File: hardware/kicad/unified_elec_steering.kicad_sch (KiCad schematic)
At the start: 18 parts, among them J1 Conn_01x03, J10 Conn_01x04, J11 Conn_01x03, J13 Conn_01x03, J2 Conn_01x03, J3 Conn_01x05, J4 Conn_01x03, J5 Conn_01x03, J6 Conn_01x02, J7 Conn_01x04, J8 Conn_01x12, J9 Conn_01x04, U1 Arduino_Nano_v3.x, U2 D24V150F7

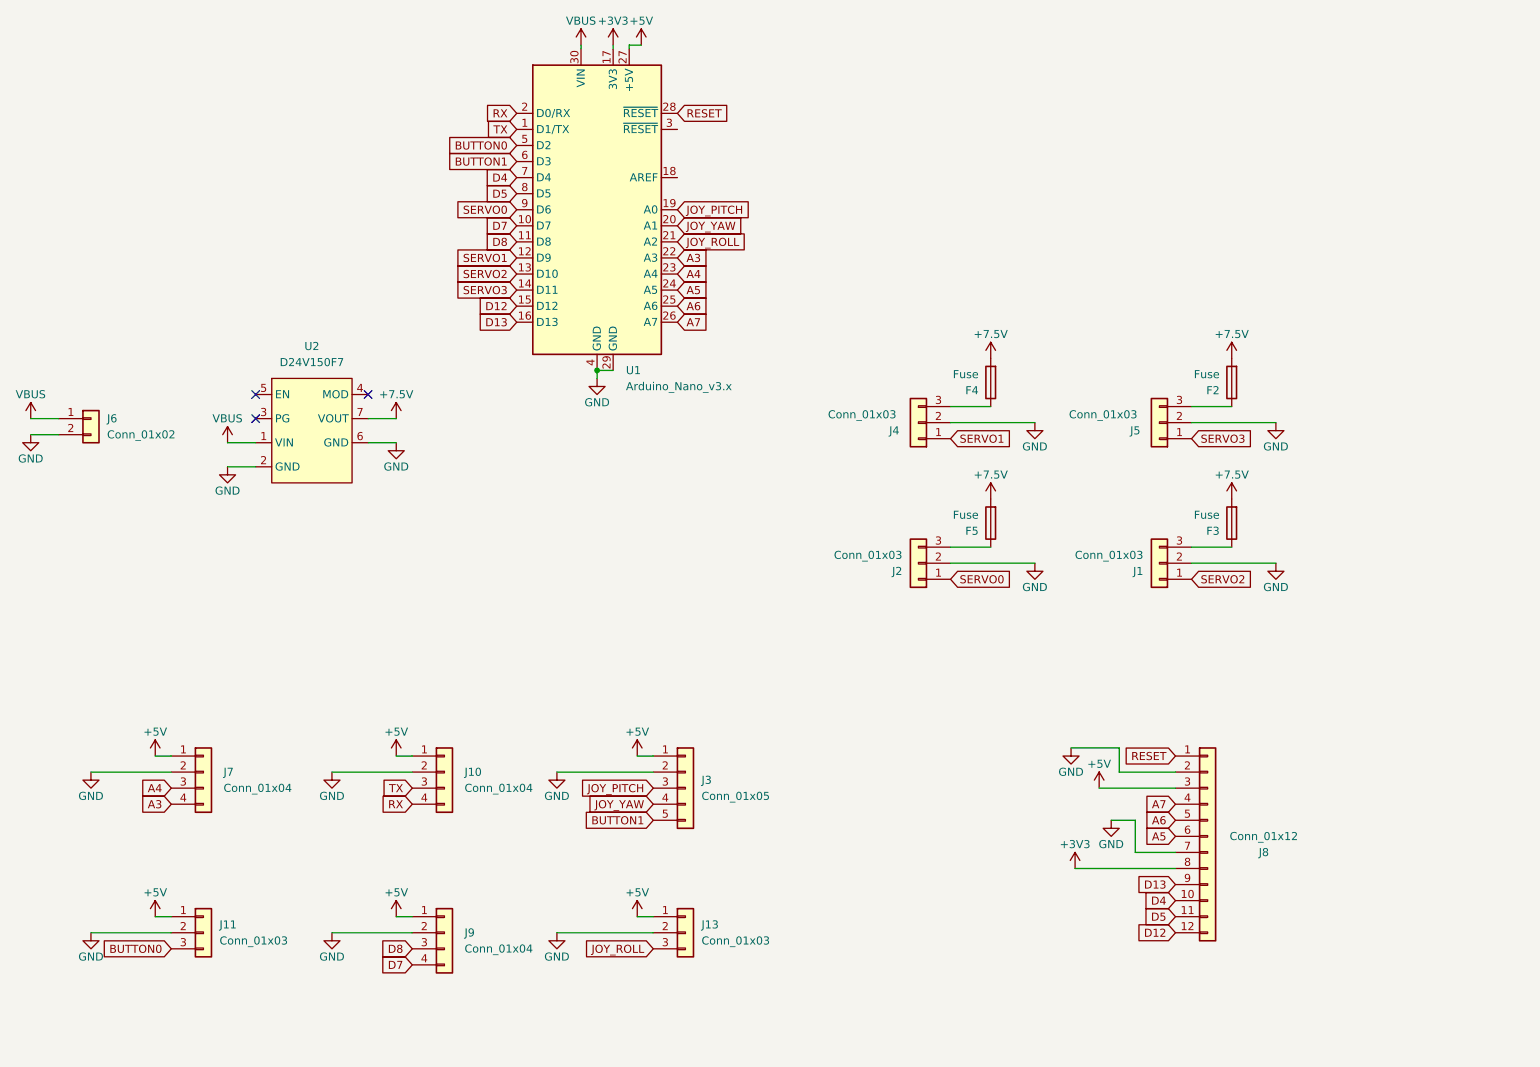
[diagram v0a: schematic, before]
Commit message: Fix schematic layout
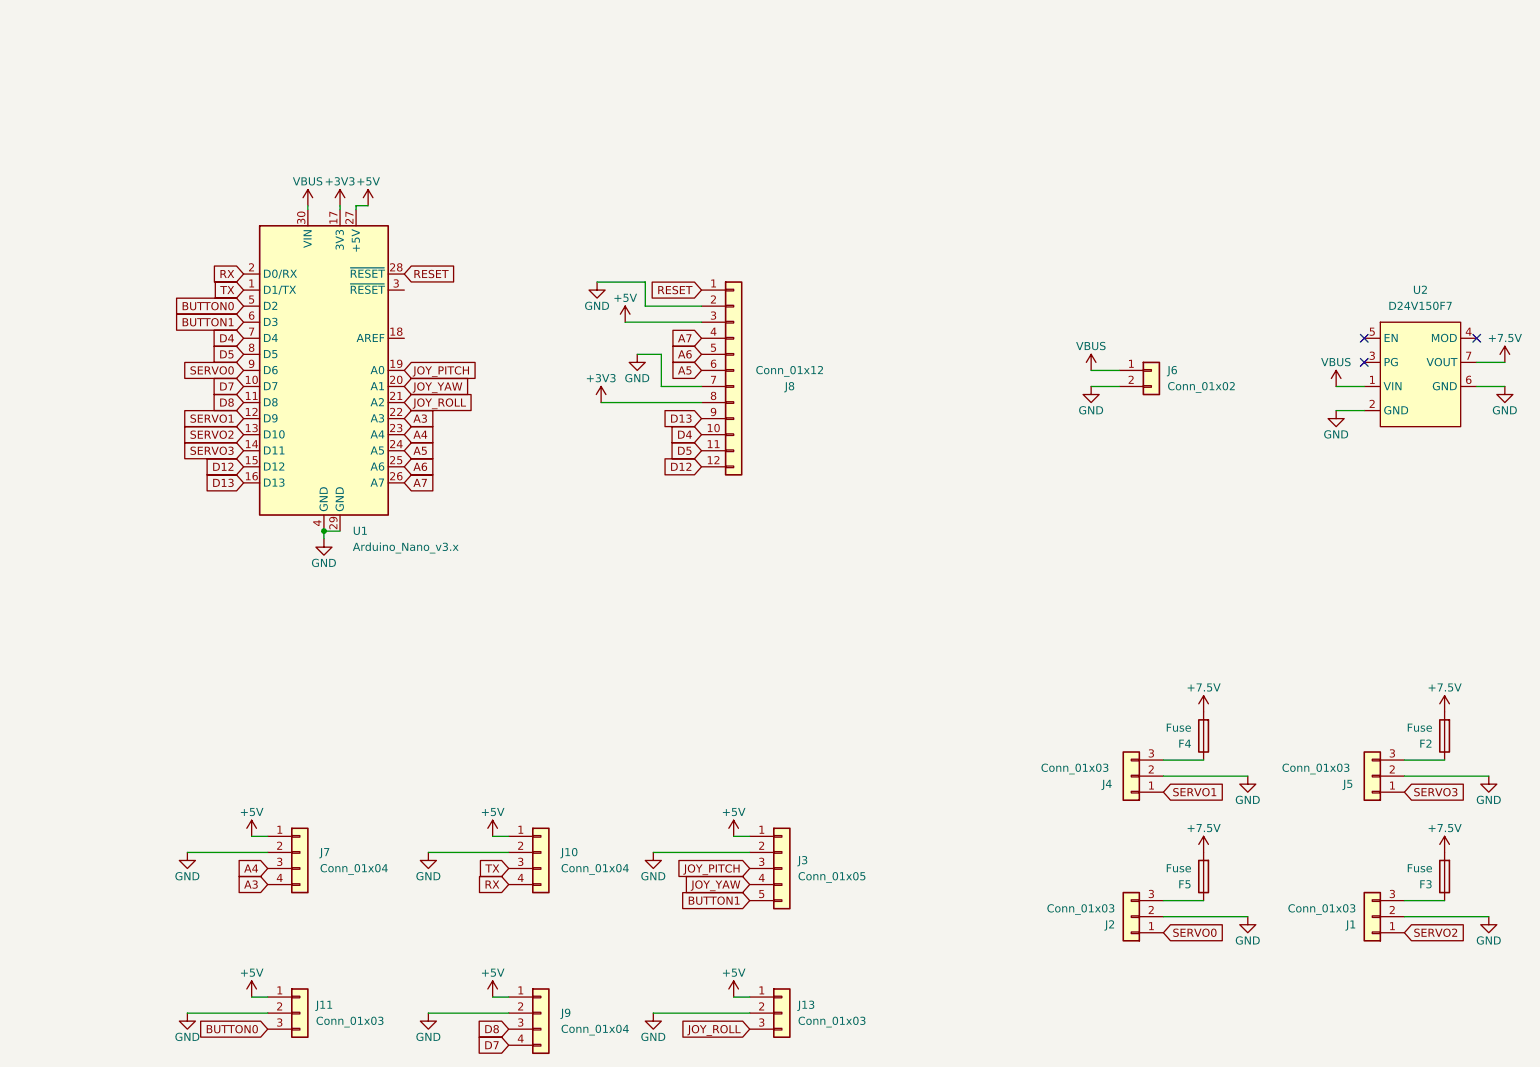
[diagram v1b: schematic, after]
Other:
- moved on the sheet: F2, F3, F4, F5, J1, J10, J11, J13, J2, J3, J4, J5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

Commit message: Initial commit of circle PCB
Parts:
- removed J3: Conn_01x05, Connector_Molex:Molex_SL_171971-0005_1x05_P2.54mm_Vertical, symbol Connector_Generic:Conn_01x05
- removed J7: Conn_01x04, Connector_Molex:Molex_SL_171971-0004_1x04_P2.54mm_Vertical, symbol Connector_Generic:Conn_01x04
- removed J8: Conn_01x12, Connector_PinHeader_2.54mm:PinHeader_1x12_P2.54mm_Vertical, symbol Connector_Generic:Conn_01x12
- added J1: Conn_01x09, Connector_PinHeader_2.54mm:PinHeader_1x09_P2.54mm_Vertical, symbol Connector_Generic:Conn_01x09
- added J7, J8: Conn_01x06, Connector_Molex:Molex_SL_171971-0006_1x06_P2.54mm_Vertical, symbol Connector_Generic:Conn_01x06
- renumbered F4 to F1, F5 to F3, F3 to F4, J1 to J10, J9 to J12, J6 to J3, J10 to J6, J2 to J9
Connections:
- net +5V: now also J7.1 (Pin_1), J8.1 (Pin_1)
- net A3: now also J8.3 (Pin_3)
- net A4: now also J7.6 (Pin_6)
- net A5: now also J7.5 (Pin_5)
- net A6: now also J7.4 (Pin_4)
- net A7: now also J7.3 (Pin_3)
- net D4: now also J12.4 (Pin_4)
- net D5: now also J12.3 (Pin_3)
- net D7: no longer J12.4 (Pin_4)
- net D8: no longer J12.3 (Pin_3)
- net GND: now also J7.2 (Pin_2), J8.2 (Pin_2)
- net RX: now also J6.3 (Pin_3); no longer J6.4 (Pin_4)
- net SERVO0: now also J10.1 (Pin_1); no longer J9.1 (Pin_1)
- net SERVO1: now also J9.1 (Pin_1); no longer J4.1 (Pin_1)
- net SERVO2: now also J5.1 (Pin_1); no longer J10.1 (Pin_1)
- net SERVO3: now also J4.1 (Pin_1); no longer J5.1 (Pin_1)
- net TX: now also J6.4 (Pin_4); no longer J6.3 (Pin_3)
- net at F2.1: now also J9.3 (Pin_3); no longer J5.3 (Pin_3)
- net at F3.1: now also J5.3 (Pin_3); no longer J9.3 (Pin_3)
- net BUTTON0 renamed D2
- net BUTTON1 renamed D3
- net D3: now also J8.6 (Pin_6)
- net JOY_PITCH renamed A0
- net A0: now also J13.3 (Pin_3)
- net JOY_ROLL renamed A2
- net A2: now also J8.4 (Pin_4); no longer J13.3 (Pin_3)
- net JOY_YAW renamed A1
- net A1: now also J8.5 (Pin_5)
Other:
- moved on the sheet: F2, F3, J11, J12, J13, J6
